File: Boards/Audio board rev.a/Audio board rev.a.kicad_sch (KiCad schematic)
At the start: 104 parts, among them J1 CEC card edge connector large, U1 6821, U10 LM324, U11 MC1458, U2 LM339, U3 LM339, U4 ULN2003A, U5 DAC-08, U6 DAC-08, U7 AH5012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

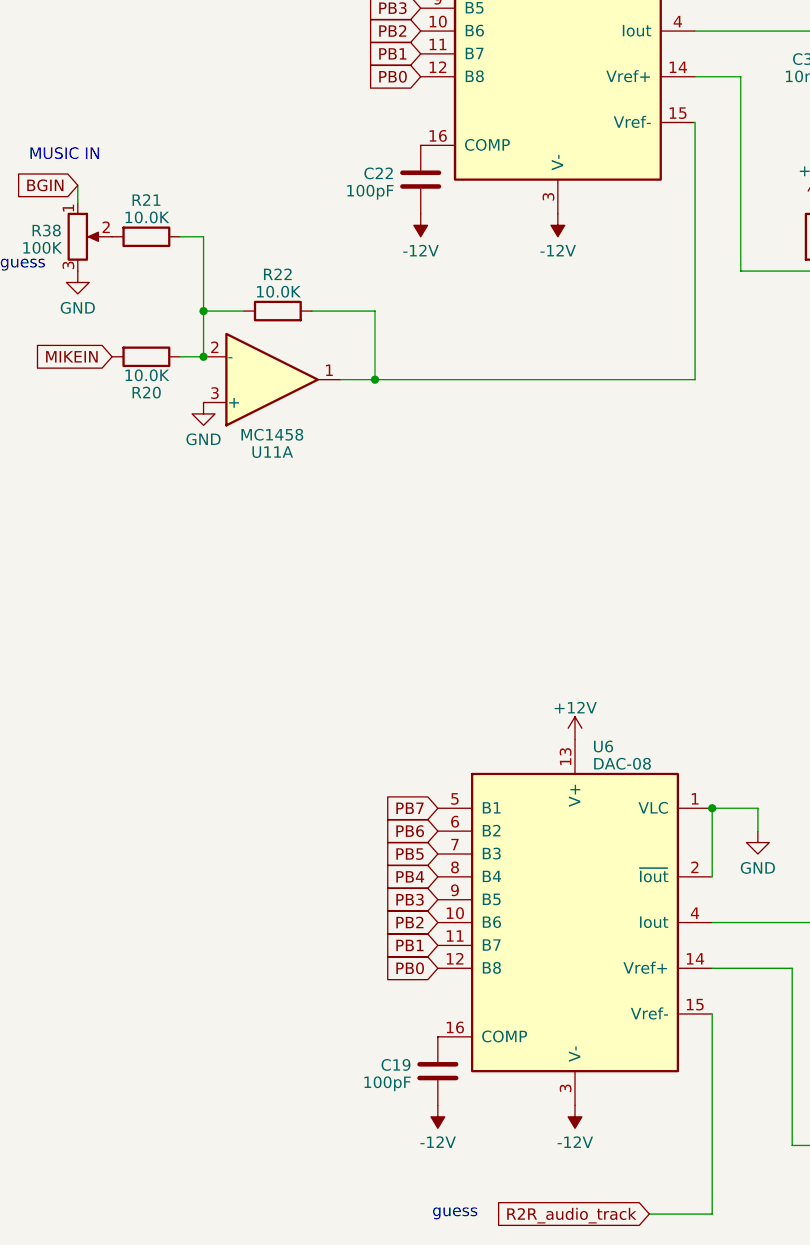
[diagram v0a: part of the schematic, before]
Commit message: U7/U9 area laid out, best guess on 0.025" grid for silk, 0.05" grid for parts
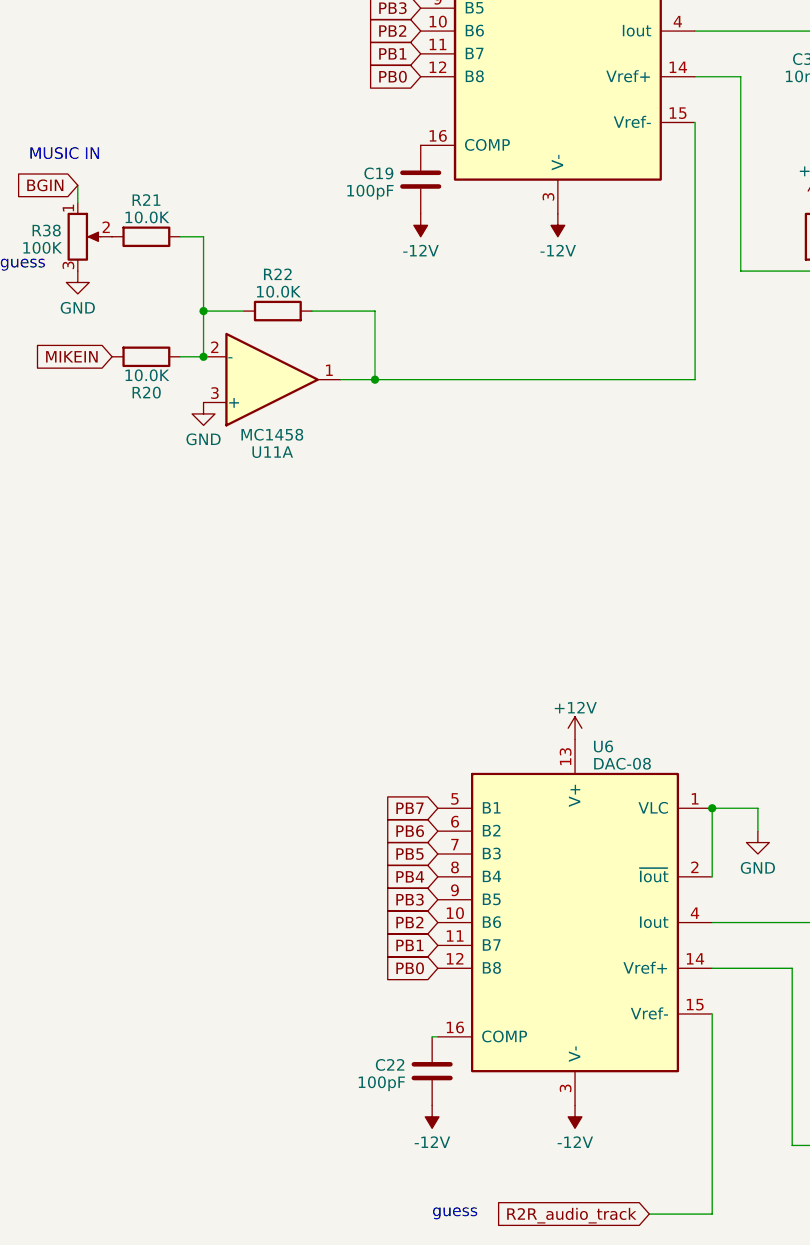
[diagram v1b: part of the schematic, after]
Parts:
- C10: footprint (none) -> Evan's parts:CP_Axial_L10.0mm_D4.5mm_P27.94mm_Horizontal
- C19, C20, C22, C23, C25, C7, C9: footprint (none) -> Capacitor_THT:C_Rect_L7.0mm_W2.5mm_P5.00mm
- R19, R34, R36, R38: footprint (none) -> Potentiometer_THT:Potentiometer_Bourns_3005_Horizontal
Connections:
- net at U6.16 (COMP): now also C22.1; no longer C19.1
- net at U5.16 (COMP): now also C19.1; no longer C22.1
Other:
- moved on the sheet: C19, C22
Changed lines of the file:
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@@
     (stroke (width 0) (type default))
   )
+  (wire (pts (xy 90.805 366.395) (xy 91.44 366.395))
+    (stroke (width 0) (type default))
+  )
   (wire (pts (xy 494.665 34.925) (xy 509.27 34.925))
     (stroke (width 0) (type default))
@@
       (effects (font (size 1.27 1.27)))
     )
-    (property "Footprint" "" (at 109.22 46.6852 0)
+    (property "Footprint" "Evan's parts:CP_Axial_L10.0mm_D4.5mm_P27.94mm_Horizontal" (at 109.22 46.6852 0)
       (effects (font (size 1.27 1.27)) hide)
     )
@@
       (effects (font (size 1.27 1.27)))
     )
-    (property "Footprint" "" (at 81.28 65.7098 0)
+    (property "Footprint" "Capacitor_THT:C_Rect_L7.0mm_W2.5mm_P5.00mm" (at 81.28 65.7098 0)
       (effects (font (size 1.27 1.27)) hide)
     )
@@
     )
   )
-  (symbol (lib_id "Device:C") (at 91.44 370.205 0) (unit 1)
+  (symbol (lib_id "Device:C") (at 89.535 271.145 0) (unit 1)
     (in_bom yes) (on_board yes) (dnp no)
-    (property "Reference" "C19" (at 88.519 369.5613 0)
+    (property "Reference" "C19" (at 86.614 270.5013 0)
       (effects (font (size 1.27 1.27)) (justify right))
     )
-    (property "Value" "100pF" (at 88.519 371.4823 0)
+    (property "Value" "100pF" (at 86.614 272.4223 0)
       (effects (font (size 1.27 1.27)) (justify right))
     )
-    (property "Footprint" "" (at 92.4052 374.015 0)
+    (property "Footprint" "Capacitor_THT:C_Rect_L7.0mm_W2.5mm_P5.00mm" (at 90.5002 274.955 0)
       (effects (font (size 1.27 1.27)) hide)
     )
-    (property "Datasheet" "~" (at 91.44 370.205 0)
+    (property "Datasheet" "~" (at 89.535 271.145 0)
       (effects (font (size 1.27 1.27)) hide)
     )
@@
       (effects (font (size 1.27 1.27)) (justify right))
     )
-    (property "Footprint" "" (at 202.565 259.715 0)
+    (property "Footprint" "Potentiometer_THT:Potentiometer_Bourns_3005_Horizontal" (at 202.565 259.715 0)
       (effects (font (size 1.27 1.27)) hide)
     )
@@
     )
   )
-  (symbol (lib_id "Device:C") (at 89.535 271.145 0) (mirror y) (unit 1)
+  (symbol (lib_id "Device:C") (at 90.805 370.205 0) (mirror y) (unit 1)
     (in_bom yes) (on_board yes) (dnp no) (fields_autoplaced)
-    (property "Reference" "C22" (at 86.614 270.5013 0)
+    (property "Reference" "C22" (at 87.884 369.5613 0)
       (effects (font (size 1.27 1.27)) (justify left))
     )
-    (property "Value" "100pF" (at 86.614 272.4223 0)
+    (property "Value" "100pF" (at 87.884 371.4823 0)
       (effects (font (size 1.27 1.27)) (justify left))
     )
-    (property "Footprint" "" (at 88.5698 274.955 0)
+    (property "Footprint" "Capacitor_THT:C_Rect_L7.0mm_W2.5mm_P5.00mm" (at 89.8398 374.015 0)
       (effects (font (size 1.27 1.27)) hide)
     )
-    (property "Datasheet" "~" (at 89.535 271.145 0)
+    (property "Datasheet" "~" (at 90.805 370.205 0)
       (effects (font (size 1.27 1.27)) hide)
     )
@@
       (effects (font (size 1.27 1.27)))
     )
-    (property "Footprint" "" (at 230.505 311.4802 0)
+    (property "Footprint" "Capacitor_THT:C_Rect_L7.0mm_W2.5mm_P5.00mm" (at 230.505 311.4802 0)
       (effects (font (size 1.27 1.27)) hide)
     )
@@
     )
   )
-  (symbol (lib_id "power:-12V") (at 89.535 274.955 0) (mirror x) (unit 1)
+  (symbol (lib_id "power:-12V") (at 90.805 374.015 0) (mirror x) (unit 1)
     (in_bom yes) (on_board yes) (dnp no) (fields_autoplaced)
-    (property "Reference" "#PWR073" (at 89.535 277.495 0)
+    (property "Reference" "#PWR073" (at 90.805 376.555 0)
       (effects (font (size 1.27 1.27)) hide)
     )
-    (property "Value" "-12V" (at 89.535 279.0905 0)
+    (property "Value" "-12V" (at 90.805 378.1505 0)
       (effects (font (size 1.27 1.27)))
     )
-    (property "Footprint" "" (at 89.535 274.955 0)
+    (property "Footprint" "" (at 90.805 374.015 0)
       (effects (font (size 1.27 1.27)) hide)
     )
-    (property "Datasheet" "" (at 89.535 274.955 0)
+    (property "Datasheet" "" (at 90.805 374.015 0)
       (effects (font (size 1.27 1.27)) hide)
     )
@@
       (effects (font (size 1.27 1.27)) (justify left))
     )
-    (property "Footprint" "" (at 161.29 338.1248 0)
+    (property "Footprint" "Capacitor_THT:C_Rect_L7.0mm_W2.5mm_P5.00mm" (at 161.29 338.1248 0)
       (effects (font (size 1.27 1.27)) hide)
     )
@@
       (effects (font (size 1.27 1.27)) (justify right))
     )
-    (property "Footprint" "" (at 277.495 319.405 0)
+    (property "Footprint" "Potentiometer_THT:Potentiometer_Bourns_3005_Horizontal" (at 277.495 319.405 0)
       (effects (font (size 1.27 1.27)) hide)
     )
@@
     )
   )
-  (symbol (lib_id "power:-12V") (at 91.44 374.015 0) (mirror x) (unit 1)
+  (symbol (lib_id "power:-12V") (at 89.535 274.955 0) (mirror x) (unit 1)
     (in_bom yes) (on_board yes) (dnp no) (fields_autoplaced)
-    (property "Reference" "#PWR074" (at 91.44 376.555 0)
+    (property "Reference" "#PWR074" (at 89.535 277.495 0)
       (effects (font (size 1.27 1.27)) hide)
     )
-    (property "Value" "-12V" (at 91.44 378.1505 0)
+    (property "Value" "-12V" (at 89.535 279.0905 0)
       (effects (font (size 1.27 1.27)))
     )
-    (property "Footprint" "" (at 91.44 374.015 0)
+    (property "Footprint" "" (at 89.535 274.955 0)
       (effects (font (size 1.27 1.27)) hide)
     )
-    (property "Datasheet" "" (at 91.44 374.015 0)
+    (property "Datasheet" "" (at 89.535 274.955 0)
       (effects (font (size 1.27 1.27)) hide)
     )
@@
       (effects (font (size 1.27 1.27)) (justify right))
     )
-    (property "Footprint" "" (at 112.395 29.845 0)
+    (property "Footprint" "Potentiometer_THT:Potentiometer_Bourns_3005_Horizontal" (at 112.395 29.845 0)
       (effects (font (size 1.27 1.27)) hide)
     )
@@
       (effects (font (size 1.27 1.27)))
     )
-    (property "Footprint" "" (at 49.53 21.2598 0)
+    (property "Footprint" "Capacitor_THT:C_Rect_L7.0mm_W2.5mm_P5.00mm" (at 49.53 21.2598 0)
       (effects (font (size 1.27 1.27)) hide)
     )
@@
       (effects (font (size 1.27 1.27)) (justify right))
     )
-    (property "Footprint" "" (at 51.435 277.495 0)
+    (property "Footprint" "Potentiometer_THT:Potentiometer_Bourns_3005_Horizontal" (at 51.435 277.495 0)
       (effects (font (size 1.27 1.27)) hide)
     )
@@
       (effects (font (size 1.27 1.27)))
     )
-    (property "Footprint" "" (at 159.385 240.3348 0)
+    (property "Footprint" "Capacitor_THT:C_Rect_L7.0mm_W2.5mm_P5.00mm" (at 159.385 240.3348 0)
       (effects (font (size 1.27 1.27)) hide)
     )

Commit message: most of layout done, fixed some bugs
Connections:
- net BGIN: now also R38.3; no longer R38.1
- net GND: now also R38.1; no longer R38.3
- net Pin 64: now also C24.2, R25.1, R30.2; no longer R25.2, U7.11
- net Pin 65: now also C21.2, R26.1, R28.1; no longer R26.2, U7.14
- net at C25.1, C26.1, R31.1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: now also R39.2
- net at C25.2, R31.2, U7.16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: no longer R39.2
- net at C10.1, R19.2, R35.1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: now also R19.1; no longer R19.3
- net at C10.2, R17.2, R18.2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: now also R19.3; no longer R19.1
- net CA2: now reaches U1.39 (CA2)
- net CA2: now also U7.15
- net CB1: no longer names the net of U1.18 (CB1)
- net CB1: no longer U7.15
- new net: R26.2, U7.14
- new net: R25.2, U7.11
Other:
- moved on the sheet: C1, C19, C2, C20, C21, C22, C23, C24, C25, C26, C3, C31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

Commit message: labeled pins 64 and 65
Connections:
- net Pin 64 renamed R2R_audio_AGC
- net Pin 65 renamed BGOUT_AGC
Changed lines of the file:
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@@
     (stroke (width 0) (type default))
   )
-  (wire (pts (xy 161.29 205.74) (xy 161.29 212.725))
+  (wire (pts (xy 161.29 198.12) (xy 161.29 212.725))
     (stroke (width 0) (type default))
   )
@@
     (stroke (width 0) (type default))
   )
-  (wire (pts (xy 161.29 205.74) (xy 167.64 205.74))
+  (wire (pts (xy 161.29 198.12) (xy 163.83 198.12))
     (stroke (width 0) (type default))
   )
@@
     )
   )
-  (global_label "Pin 65" (shape input) (at 167.64 205.74 0) (fields_autoplaced)
-    (effects (font (size 1.27 1.27)) (justify left))
-    (property "Intersheetrefs" "${INTERSHEET_REFS}" (at 176.9562 205.74 0)
-      (effects (font (size 1.27 1.27)) (justify left) hide)
-    )
-  )
-  (global_label "Pin 64" (shape input) (at 163.195 327.025 0) (fields_autoplaced)
-    (effects (font (size 1.27 1.27)) (justify left))
-    (property "Intersheetrefs" "${INTERSHEET_REFS}" (at 172.5112 327.025 0)
+  (global_label "BGOUT_AGC" (shape input) (at 163.83 198.12 0) (fields_autoplaced)
+    (effects (font (size 1.27 1.27)) (justify left))
+    (property "Intersheetrefs" "${INTERSHEET_REFS}" (at 177.5006 198.12 0)
+      (effects (font (size 1.27 1.27)) (justify left) hide)
+    )
+  )
+  (global_label "R2R_audio_AGC" (shape input) (at 163.195 327.025 0) (fields_autoplaced)
+    (effects (font (size 1.27 1.27)) (justify left))
+    (property "Intersheetrefs" "${INTERSHEET_REFS}" (at 180.6149 327.025 0)
       (effects (font (size 1.27 1.27)) (justify left) hide)
     )
@@
     )
   )
-  (global_label "Pin 64" (shape input) (at 481.965 34.925 180) (fields_autoplaced)
-    (effects (font (size 1.27 1.27)) (justify right))
-    (property "Intersheetrefs" "${INTERSHEET_REFS}" (at 472.6488 34.925 0)
+  (global_label "R2R_audio_AGC" (shape input) (at 481.965 34.925 180) (fields_autoplaced)
+    (effects (font (size 1.27 1.27)) (justify right))
+    (property "Intersheetrefs" "${INTERSHEET_REFS}" (at 464.5451 34.925 0)
       (effects (font (size 1.27 1.27)) (justify right) hide)
     )
@@
     )
   )
-  (global_label "Pin 65" (shape input) (at 481.965 37.465 180) (fields_autoplaced)
-    (effects (font (size 1.27 1.27)) (justify right))
-    (property "Intersheetrefs" "${INTERSHEET_REFS}" (at 472.6488 37.465 0)
-      (effects (font (size 1.27 1.27)) (justify right) hide)
-    )
+  (global_label "BGOUT_AGC" (shape input) (at 481.965 37.465 180) (fields_autoplaced)
+    (effects (font (size 1.27 1.27)) (justify right))
+    (property "Intersheetrefs" "${INTERSHEET_REFS}" (at 468.2944 37.465 0)
+      (effects (font (size 1.27 1.27)) (justify right) hide)
+    )
